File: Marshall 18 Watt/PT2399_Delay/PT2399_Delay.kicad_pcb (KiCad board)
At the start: 2 copper layers, 52 parts, among them J1 IN, J2 +9V, J3 IN, U1 PT2399, U2 TL072, U3 L7805

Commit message: Update _26_03_25
PCB
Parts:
- added D2: IR204A, LED_THT:LED_D3.0mm_IRBlack, F.Cu at (58.4, 36.2)
- added J4: IN, Connector_JST:JST_XA_B02B-XASK-1_1x02_P2.50mm_Vertical, F.Cu at (54.6, 54.6)
- added R21: 10k, Resistor_THT:R_Axial_DIN0204_L3.6mm_D1.6mm_P5.08mm_Horizontal, F.Cu at (63.5, 40.6)
- C14, C5, C6: footprint Capacitor_THT:CP_Radial_D4.0mm_P2.00mm -> Capacitor_THT:CP_Radial_D5.0mm_P2.50mm
- FDBK1, FDBK2, MIX1: footprint Potentiometer_THT:Potentiometer_Alps_RK163_Single_Horizontal -> Potentiometer_THT:Potentiometer_Omeg_PC16BU_Vertical; moved to B.Cu
- J2: value +9V -> Barrel_Jack_Switch
- moved D1 67.2 mm to (78.7, 48.3), turned to 180 degrees
- moved R8 64.4 mm to (88.3, 88.3), turned to 180 degrees
- moved R16 62.9 mm to (94.0, 88.3)
- moved J3 61.2 mm to (54.0, 73.0), turned to 90 degrees
- moved J2 58.6 mm to (78.7, 40.6), turned to 180 degrees
- moved R20 57.0 mm to (73.7, 66.0)
- moved R3 56.6 mm to (59.1, 59.5)
- moved R10 56.3 mm to (88.3, 85.1), turned to 180 degrees
- moved C1 55.6 mm to (61.0, 71.1)
- moved C2 54.9 mm to (61.0, 74.3)
- moved R9 54.4 mm to (78.7, 71.1), turned to 180 degrees
- moved R11 53.0 mm to (83.2, 80.0)
- moved R18 52.6 mm to (94.0, 81.9)
- moved C5 52.1 mm to (62.2, 46.4), turned to 180 degrees
- moved C10 51.7 mm to (53.3, 77.5), turned to -90 degrees
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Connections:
- J2 pad 3: (no net) -> GND
- U1 pad 1: unconnected-(U1-VCC-Pad1) -> VDD
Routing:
- net Net-(U1-OP2-OUT): track 0.00 -> 34.1 mm
- net Vref: track 0.00 -> 29.5 mm
- net Net-(U1-LPF2-IN): track 0.00 -> 28.6 mm
- net Net-(U2A--): track 0.00 -> 23.9 mm
- net Net-(U1-LPF2-OUT): track 0.00 -> 20.9 mm
- net VDD: track 0.00 -> 20.8 mm
- net Net-(U1-VCO): track 0.00 -> 20.8 mm
- net Net-(U1-LPF1-OUT): track 0.00 -> 17.9 mm
- net Net-(D1-K): track 0.00 -> 17.2 mm
- net Net-(C15-Pad2): track 0.00 -> 16.3 mm
- net Net-(C8-Pad2): track 0.00 -> 16.2 mm
- net Net-(U1-OP1-IN): track 0.00 -> 15.6 mm
- net Net-(C19-Pad2): track 0.00 -> 14.0 mm
- net Net-(U2B--): track 0.00 -> 13.4 mm
- net GNDA: track 0.00 -> 13.2 mm
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- added copper zone on B.Cu, net GND

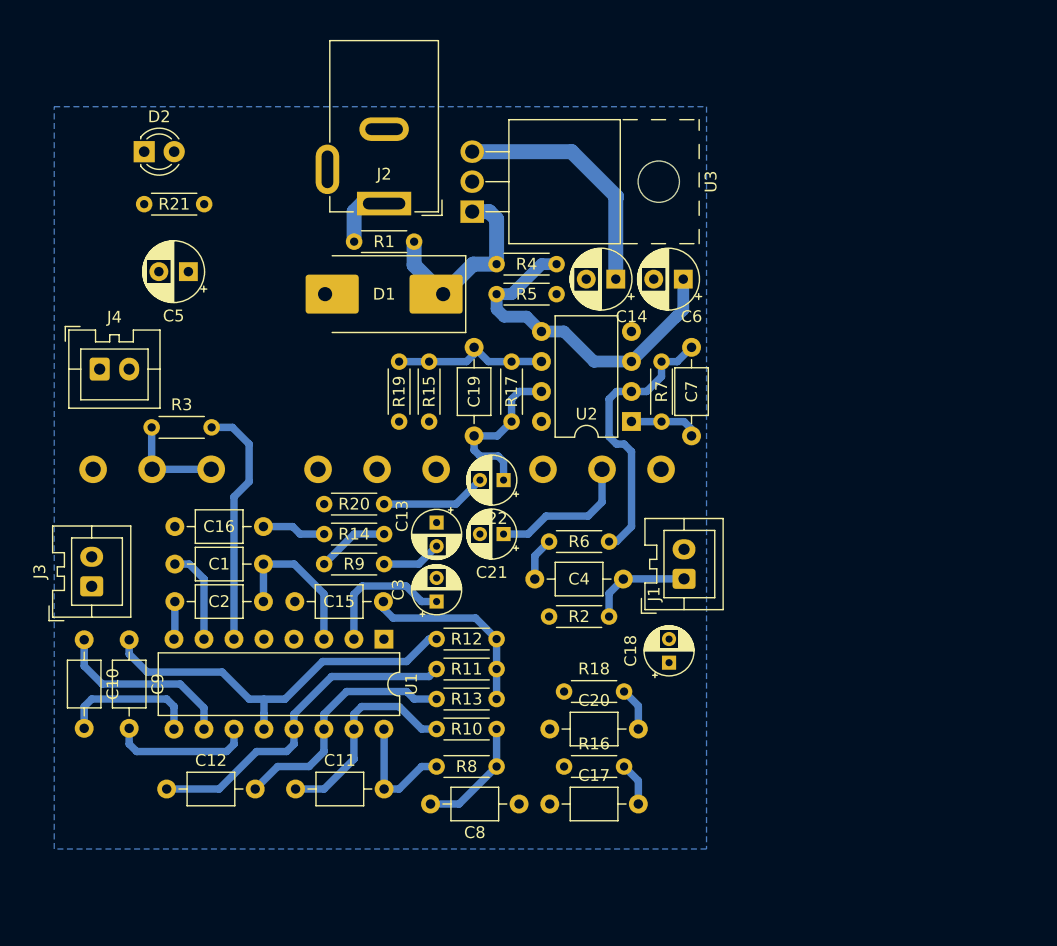
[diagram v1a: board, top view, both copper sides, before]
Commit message: update_27_03_25
add distortion
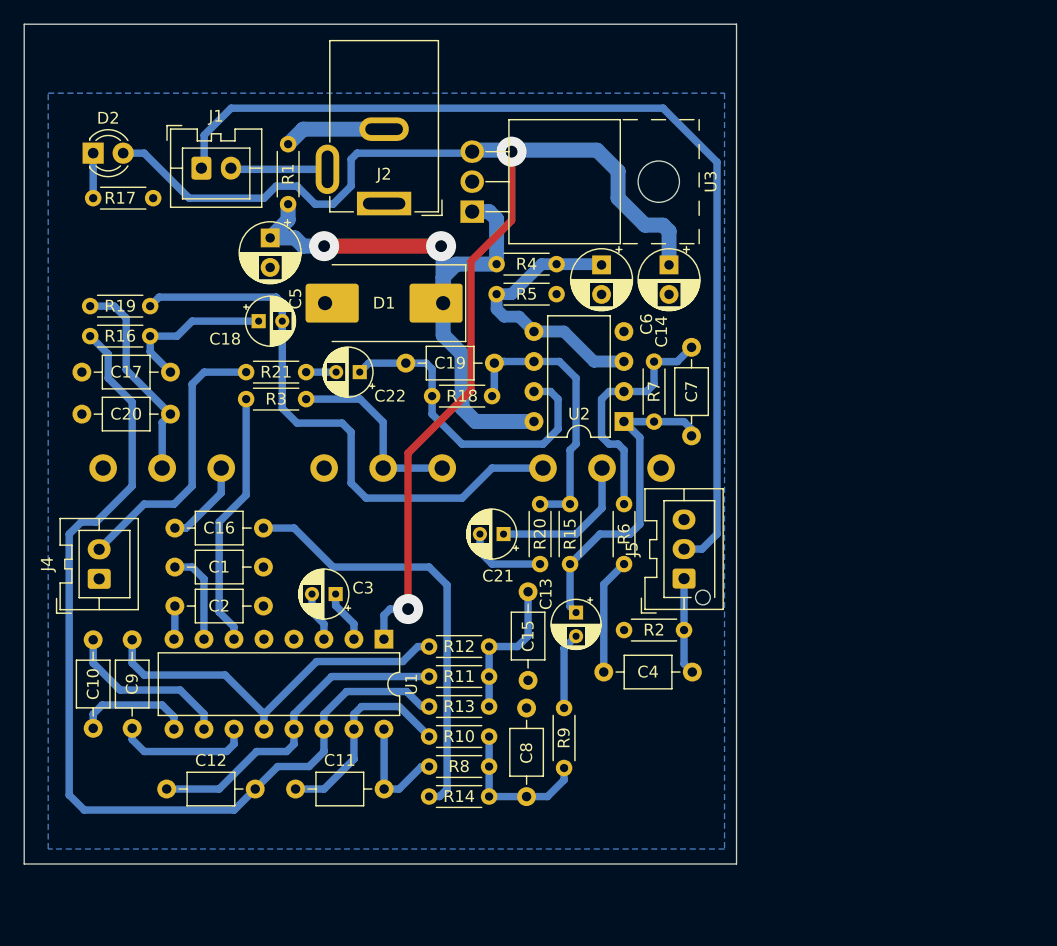
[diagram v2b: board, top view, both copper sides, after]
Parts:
- removed FDBK2: 50K, Potentiometer_THT:Potentiometer_Omeg_PC16BU_Vertical
- removed J3: IN, Connector_JST:JST_XA_B02B-XASK-1_1x02_P2.50mm_Vertical
- added DELAY1: 50K, Potentiometer_THT:Potentiometer_Omeg_PC16BU_Vertical, B.Cu at (73.7, 63.0)
- added J5: IN, Connector_JST:JST_XA_B03B-XASK-1-A_1x03_P2.50mm_Vertical, F.Cu at (104.1, 72.3)
- R17: value 12K -> 10k
- R18: value 2K -> 12K
- R19: value 20K -> 2K
- R20: value 1K -> 20K
- R21: value 10k -> 1K
- moved R16 54.2 mm to (53.8, 51.8)
- moved C17 53.9 mm to (53.1, 54.9)
- moved J1 53.7 mm to (63.3, 37.6), turned to 0 degrees
- moved C20 47.8 mm to (53.1, 58.4)
- moved C18 45.2 mm to (68.1, 50.5), turned to 0 degrees
- moved R17 35.8 mm to (59.2, 40.1), turned to 180 degrees
- moved R18 27.4 mm to (82.8, 56.9)
- moved R14 23.9 mm to (82.5, 90.8)
- moved R19 23.2 mm to (58.9, 49.3), turned to 180 degrees
- moved C15 20.8 mm to (90.9, 81.0), turned to 90 degrees
- moved R9 19.5 mm to (94.0, 83.3), turned to -90 degrees
- moved R20 19.0 mm to (91.9, 71.1), turned to 90 degrees
- moved J4 17.8 mm to (54.6, 72.4), turned to 90 degrees
- moved R15 17.0 mm to (94.5, 66.0)
- moved C22 15.2 mm to (76.7, 54.9)
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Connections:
- C1 pad 2: GNDA -> GND
- C2 pad 2: GNDA -> GND
- C3 pad 2: GNDA -> GND
- C4 pad 1: Net-(J1-Pin_1) -> Net-(J5-Pin_1)
- FDBK1 pad 2: Net-(FDBK1-Pad2) -> Net-(C20-Pad2)
- FDBK1 pad 3: Net-(FDBK1-Pad2) -> Net-(C16-Pad1)
- J1 pad 2: GNDA -> Net-(J1-Pin_2)
- J2 pad 1: Net-(J2-Pad1) -> GND
- J2 pad 2: GND -> Net-(J2-Pad2)
- J2 pad 3: GND -> Net-(J1-Pin_2)
- J4 pad 1: GNDA -> GND
- J4 pad 2: GND -> Net-(J4-Pin_2)
- R1 pad 1: Net-(J2-Pad1) -> Net-(J2-Pad2)
- R17 pad 1: Net-(C19-Pad2) -> GND
- R17 pad 2: Net-(U2B--) -> Net-(D2-K)
- R18 pad 1: Net-(C18-Pad2) -> Net-(C19-Pad2)
- R18 pad 2: Net-(C20-Pad2) -> Net-(U2B--)
- R19 pad 1: Net-(C21-Pad2) -> Net-(C18-Pad2)
- R19 pad 2: Net-(U2B--) -> Net-(C20-Pad2)
- R2 pad 2: Net-(J1-Pin_1) -> Net-(J5-Pin_1)
- R20 pad 1: Net-(J3-Pin_2) -> Net-(C21-Pad2)
- R20 pad 2: Net-(C22-Pad2) -> Net-(U2B--)
- R21 pad 1: GND -> Net-(J4-Pin_2)
- R21 pad 2: Net-(D2-K) -> Net-(C22-Pad2)
- R3 pad 1: Net-(FDBK1-Pad2) -> Net-(DELAY1-Pad2)
- U1 pad 3: GNDA -> GND
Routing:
- net VDD: track 20.8 -> 105.9 mm, vias 0 -> 2
- net Net-(J1-Pin_1): track 8.19 -> 84.0 mm
- net Net-(U1-LPF2-OUT): track 20.9 -> 80.2 mm
- net Net-(C18-Pad2): track 0.00 -> 49.4 mm
- net Net-(D1-K): track 17.2 -> 53.8 mm, vias 0 -> 2
- net Net-(C16-Pad2): track 5.40 -> 36.6 mm
- net Net-(J4-Pin_2): track 0.00 -> 23.7 mm
- net Net-(C13-Pad1): track 5.93 -> 26.8 mm
- net Net-(DELAY1-Pad2): track 0.00 -> 16.2 mm
- net Net-(C20-Pad2): track 3.68 -> 18.1 mm
- net Net-(C19-Pad2): track 14.0 -> 27.6 mm
- net GNDA: track 13.2 -> 0.00 mm
- net Net-(U2B--): track 13.4 -> 23.4 mm
- net Net-(C17-Pad2): track 3.68 -> 13.5 mm
- net Net-(J2-Pad2): track 0.00 -> 8.65 mm
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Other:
- board outline added: 60.3 x 71.1 mm
